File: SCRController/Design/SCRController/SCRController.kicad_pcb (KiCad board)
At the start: 2 copper layers, 100 x 100 mm, 24 parts, among them Q1 2N2907A, Q2 2N2222A, Q3 2N2222A, Q4 2N2907A, U1 TL084, U2 TL084

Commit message: Updated footprints
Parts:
- added C2: C, Capacitor_THT:C_Radial_D4.0mm_H5.0mm_P1.50mm, F.Cu at (160.6, 64.2)
- added C4: C, Capacitor_THT:C_Radial_D4.0mm_H5.0mm_P1.50mm, F.Cu at (160.6, 69.8)
- added C5: C, Capacitor_THT:C_Radial_D4.0mm_H5.0mm_P1.50mm, F.Cu at (160.6, 75.3)
- added C6: C, Capacitor_THT:C_Radial_D4.0mm_H5.0mm_P1.50mm, F.Cu at (160.6, 80.9)
- added D1: KBPC1501W, PCM_Diode_THT_AKL:Diode_Bridge_KBP, F.Cu at (178.0, 94.1)
- added J1: VALT, TerminalBlock:TerminalBlock_MaiXu_MX126-5.0-03P_1x03_P5.00mm, F.Cu at (179.8, 76.6)
- added J2: SAL_TRIAC, TerminalBlock:TerminalBlock_MaiXu_MX126-5.0-02P_1x02_P5.00mm, F.Cu at (179.8, 66.5)
- added R1: 20k, Resistor_THT:R_Axial_DIN0207_L6.3mm_D2.5mm_P7.62mm_Horizontal, F.Cu at (149.4, 63.5)
- added R11: 10k, Resistor_THT:R_Axial_DIN0207_L6.3mm_D2.5mm_P7.62mm_Horizontal, F.Cu at (149.1, 88.2)
- added R2: 20k, Resistor_THT:R_Axial_DIN0207_L6.3mm_D2.5mm_P7.62mm_Horizontal, F.Cu at (149.4, 67.5)
- added R5: 10k, Resistor_THT:R_Axial_DIN0207_L6.3mm_D2.5mm_P7.62mm_Horizontal, F.Cu at (149.4, 71.6)
- added R6: 10k, Resistor_THT:R_Axial_DIN0207_L6.3mm_D2.5mm_P7.62mm_Horizontal, F.Cu at (149.4, 75.6)
- added R7: 220, Resistor_THT:R_Axial_DIN0207_L6.3mm_D2.5mm_P7.62mm_Horizontal, F.Cu at (149.4, 79.7)
- added R8: 1K, Resistor_THT:R_Axial_DIN0207_L6.3mm_D2.5mm_P7.62mm_Horizontal, F.Cu at (149.4, 83.7)
- added U3: LM7815_TO220, Package_TO_SOT_THT:TO-220-3_Vertical, F.Cu at (167.4, 87.2)
- added U4: LM7915_TO220, Package_TO_SOT_THT:TO-220-3_Vertical, F.Cu at (167.4, 93.2)
- added U5: MOC3011M, PCM_Package_DIP_AKL:DIP-6_W7.62mm_LongPads, F.Cu at (177.8, 83.7)
- U2: footprint Package_DIP:CERDIP-14_W7.62mm_SideBrazed -> PCM_Package_DIP_AKL:DIP-14_W7.62mm_LongPads
- moved U2 21.9 mm to (166.2, 64.8)
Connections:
- net Earth renamed DERCENT
- U1 pad 11: (no net) -> VEE
- U1 pad 4: (no net) -> VCC
- U2 pad 1: (no net) -> SUM
- U2 pad 11: unconnected-(U2E-V--Pad11) -> VEE
- U2 pad 2: (no net) -> Net-(U2A--)
- U2 pad 3: (no net) -> Net-(U2A-+)
- U2 pad 4: unconnected-(U2E-V+-Pad4) -> VCC

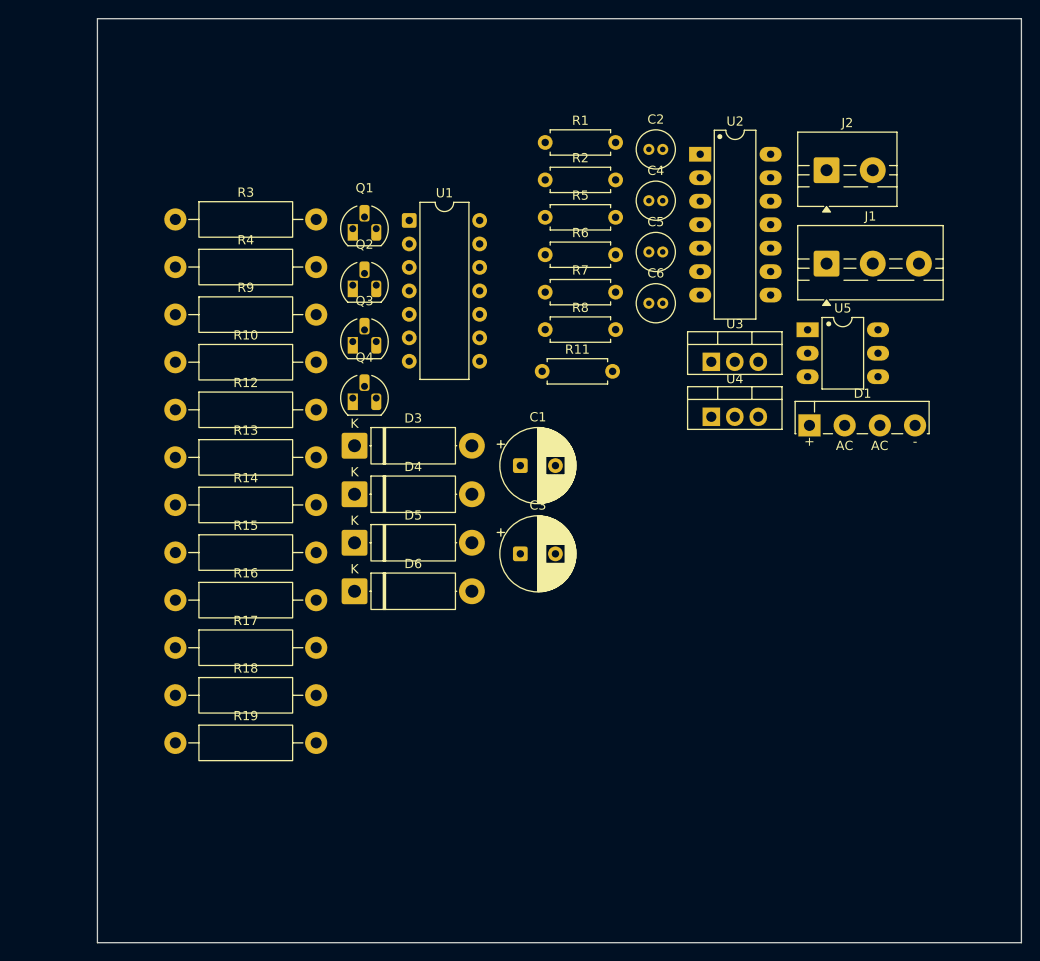
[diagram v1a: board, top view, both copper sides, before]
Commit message: Updated Footprints
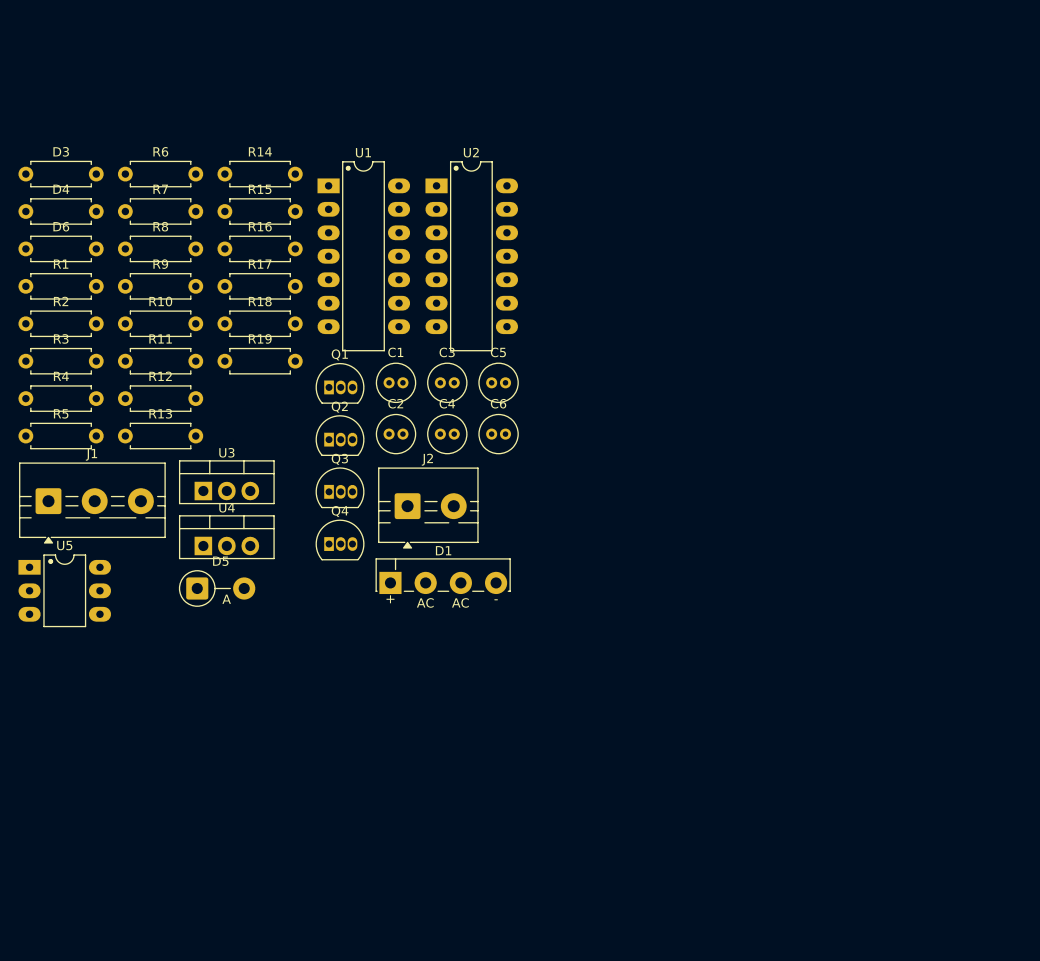
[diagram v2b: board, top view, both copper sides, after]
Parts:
- C1, C3: footprint Capacitor_THT:CP_Radial_D8.0mm_P3.80mm -> Capacitor_THT:C_Radial_D4.0mm_H5.0mm_P1.50mm
- D3, D4, D6: footprint Diode_THT:D_5W_P12.70mm_Horizontal -> Resistor_THT:R_Axial_DIN0207_L6.3mm_D2.5mm_P7.62mm_Horizontal
- D5: footprint Diode_THT:D_5W_P12.70mm_Horizontal -> Diode_THT:D_DO-15_P5.08mm_Vertical_AnodeUp
- Q1, Q2, Q3, Q4: footprint Package_TO_SOT_THT:TO-92_HandSolder -> Package_TO_SOT_THT:TO-92L_Inline
- R10, R12, R13, R14, R15, R16, R17, R18, R19, R3, R4, R9: footprint Resistor_THT:R_Axial_DIN0411_L9.9mm_D3.6mm_P15.24mm_Horizontal -> Resistor_THT:R_Axial_DIN0207_L6.3mm_D2.5mm_P7.62mm_Horizontal
- U1: footprint Package_DIP:CERDIP-14_W7.62mm_SideBrazed -> PCM_Package_DIP_AKL:DIP-14_W7.62mm_LongPads
- moved J1 88.0 mm to (95.6, 102.3)
- moved U5 88.0 mm to (93.6, 109.5)
- moved R5 61.0 mm to (93.2, 95.2)
- moved R1 58.3 mm to (93.2, 79.0)
- moved R2 58.3 mm to (93.2, 83.1)
- moved J2 58.1 mm to (134.5, 102.8)
- moved U3 56.7 mm to (112.4, 101.2)
- moved U4 56.7 mm to (112.4, 107.2)
- moved D6 51.4 mm to (93.2, 75.0)
- moved D1 48.4 mm to (132.6, 111.2)
- moved D4 46.9 mm to (93.2, 71.0)
- moved R6 46.3 mm to (104.0, 66.9)
- moved R7 46.3 mm to (104.0, 71.0)
- moved R8 46.3 mm to (104.0, 75.0)
- moved D3 46.1 mm to (93.2, 66.9)
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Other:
- board outline removed

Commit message: Update SCRController design files
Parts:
- added RV1: R_Potentiometer_US, Potentiometer_THT:Potentiometer_Alps_RK09Y11_Single_Horizontal, F.Cu at (82.0, 93.0)
- moved J1 38.1 mm to (78.0, 68.5)
- moved D5 15.6 mm to (108.3, 127.0)
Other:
- board outline added: 100 x 100 mm

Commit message: Changed FP
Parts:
- D3, D4, D6: footprint Resistor_THT:R_Axial_DIN0207_L6.3mm_D2.5mm_P7.62mm_Horizontal -> Diode_THT:D_DO-15_P5.08mm_Vertical_AnodeUp
- moved D4 20.9 mm to (110.9, 59.8)
- moved D3 6.77 mm to (94.0, 60.2)

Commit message: Placed Footprints and first routed
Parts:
- moved J1 85.0 mm to (161.1, 86.3), turned to 90 degrees
- moved U5 80.3 mm to (142.6, 45.9)
- moved U4 64.3 mm to (162.1, 66.3), turned to 90 degrees
- moved J2 59.4 mm to (157.8, 48.2)
- moved R5 58.4 mm to (126.0, 47.0)
- moved R8 49.3 mm to (149.0, 95.0)
- moved R7 47.1 mm to (141.0, 100.0)
- moved R11 46.6 mm to (145.1, 65.3), turned to 90 degrees
- moved D5 40.6 mm to (125.0, 90.0)
- moved Q3 37.6 mm to (113.0, 66.0)
- moved R2 35.2 mm to (96.0, 48.0)
- moved C1 35.2 mm to (97.7, 94.7)
- moved R16 35.2 mm to (110.8, 110.0)
- moved C5 34.5 mm to (148.2, 55.2)
- moved R19 30.2 mm to (117.0, 57.0)
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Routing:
- net DERCENT: track 0.00 -> 405.7 mm
- net VCC: track 0.00 -> 388.7 mm
- net VDC-: track 0.00 -> 87.7 mm
- net VCOMP: track 0.00 -> 87.7 mm
- net Net-(D3-A): track 0.00 -> 79.6 mm
- net VEE: track 0.00 -> 60.1 mm
- net Net-(Q2-C): track 0.00 -> 58.9 mm
- net VSync: track 0.00 -> 51.4 mm
- net VA+: track 0.00 -> 46.3 mm
- net Net-(U2A-+): track 0.00 -> 45.2 mm
- net Net-(Q3-C): track 0.00 -> 42.3 mm
- net VA-: track 0.00 -> 34.0 mm
- net Net-(Q1-B): track 0.00 -> 31.3 mm
- net Net-(R11-Pad1): track 0.00 -> 28.6 mm
- net A1: track 0.00 -> 28.1 mm
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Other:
- board size 100 x 100 mm -> 74.7 x 71.8 mm

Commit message: Pcb full
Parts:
- moved J1 4.89 mm to (156.2, 86.3)
- moved C6 3.92 mm to (147.8, 80.2), turned to 90 degrees
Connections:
- U4 pad 1: unconnected-(U4-GND-Pad1) -> DERCENT
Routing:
- net VCC: track 388.7 -> 404.4 mm
- net VEE: track 60.1 -> 48.6 mm
- net DERCENT: track 405.7 -> 415.4 mm
- net VDC-: track 87.7 -> 94.3 mm
- net VA+: track 46.3 -> 52.6 mm
- added copper zone on B.Cu, net DERCENT

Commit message: Correcciones
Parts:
- added R20: 10k, Resistor_THT:R_Axial_DIN0207_L6.3mm_D2.5mm_P7.62mm_Horizontal, F.Cu at (72.2, 32.8)
- C2, C5: value C -> 2200uF
- C4, C6: value C -> 0.1uF
- RV1: value R_Potentiometer_US -> 5K; footprint Potentiometer_THT:Potentiometer_Alps_RK09Y11_Single_Horizontal -> Potentiometer_THT:Potentiometer_Alps_RK163_Single_Horizontal
- moved C5 66.4 mm to (86.4, 31.0), turned to -90 degrees
- moved RV1 66.0 mm to (35.8, 48.8)
- moved C1 65.5 mm to (36.4, 71.8)
- moved C2 65.5 mm to (75.7, 72.0)
- moved C3 65.5 mm to (54.2, 75.5)
- moved C4 65.5 mm to (81.7, 72.0)
- moved C6 65.5 mm to (86.5, 57.3)
- moved D3 65.5 mm to (49.7, 23.0)
- moved D4 65.5 mm to (36.1, 35.2)
- moved D5 65.5 mm to (63.7, 67.0)
- moved D6 65.5 mm to (46.7, 37.0)
- moved Q1 65.5 mm to (41.7, 72.0)
- moved Q3 65.5 mm to (51.7, 43.0)
- moved R1 65.5 mm to (34.7, 30.0)
- moved R10 65.5 mm to (47.7, 71.0)
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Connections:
- net DERCENT renamed Earth
- D1 pad 3: VDC- -> VA+
- D1 pad 4: VA+ -> VDC-
- U5 pad 1: SUM -> Net-(R20-Pad2)
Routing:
- net VCC: track 404.4 -> 436.5 mm
- net Net-(R20-Pad2): track 0.00 -> 14.1 mm
- net SUM: track 27.6 -> 18.2 mm
- net Net-(Q2-C): track 58.9 -> 67.6 mm
- net Net-(U2A-+): track 45.2 -> 53.5 mm
- net VA+: track 52.6 -> 47.0 mm
- net VA-: track 34.4 -> 39.9 mm
- net Earth: track 415.4 -> 420.4 mm
- net Net-(Q1-C): track 14.1 -> 18.0 mm
- net Net-(Q3-C): track 42.3 -> 45.1 mm
- net Net-(D3-A): track 79.6 -> 81.7 mm
- net Net-(D4-A): track 19.9 -> 22.0 mm
- net Net-(Q4-E): track 13.9 -> 15.8 mm
- net VEE: track 48.6 -> 50.4 mm
- net Net-(Q1-B): track 31.3 -> 32.6 mm
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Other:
- board size 74.7 x 71.8 mm -> 76.9 x 73 mm

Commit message: rehecho
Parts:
- moved R2 58.7 mm to (80.5, 61.8), turned to 90 degrees
- moved R9 56.6 mm to (83.7, 70.0), turned to -90 degrees
- moved D3 53.0 mm to (84.3, 63.2), turned to 90 degrees
- moved R1 45.3 mm to (80.0, 31.2), turned to -90 degrees
- moved R14 43.0 mm to (61.9, 29.1), turned to -135 degrees
- moved Q2 36.7 mm to (52.3, 29.9), turned to 180 degrees
- moved D5 34.0 mm to (67.3, 33.2), turned to -90 degrees
- moved D4 31.0 mm to (52.8, 61.4), turned to 90 degrees
- moved R17 30.0 mm to (76.9, 75.7), turned to 90 degrees
- moved R5 29.5 mm to (90.4, 38.6), turned to 180 degrees
- moved R4 29.3 mm to (52.2, 65.2)
- moved U3 27.9 mm to (102.7, 55.2), turned to 90 degrees
- moved C4 25.6 mm to (95.1, 50.2), turned to -90 degrees
- moved R13 25.3 mm to (53.9, 87.0), turned to 90 degrees
- moved C2 25.2 mm to (96.2, 57.3), turned to 90 degrees
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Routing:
- net VCC: track 436.5 -> 190.9 mm
- net VSync: track 51.4 -> 176.6 mm
- net Net-(D3-A): track 81.7 -> 19.1 mm
- net Earth: track 420.4 -> 452.9 mm
- net A2: track 25.1 -> 55.7 mm
- net VA-: track 39.9 -> 10.8 mm
- net Net-(Q3-C): track 45.1 -> 17.4 mm
- net Net-(R11-Pad1): track 29.4 -> 4.01 mm
- net VA+: track 47.0 -> 22.4 mm
- net VCOMP: track 86.8 -> 105.9 mm
- net VDC-: track 93.7 -> 75.2 mm
- net Net-(U2A--): track 23.1 -> 41.4 mm
- net Net-(D4-A): track 22.0 -> 4.85 mm
- net A1: track 28.1 -> 11.4 mm
- net VEE: track 50.4 -> 65.9 mm
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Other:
- board size 76.9 x 73 mm -> 77.6 x 73.5 mm
